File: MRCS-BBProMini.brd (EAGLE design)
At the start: 72.4 x 33.3 mm, 10 parts

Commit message: fixed silkscreen
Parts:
- BBLEO: value (none) -> Footprint
- C1: device SPCoast:e5-10.5 -> SPCoast:E5-10.5
- J1: value (none) -> 2.1mm
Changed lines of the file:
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@@
 <setting verticaltext="up"/>
 </settings>
-<grid distance="50" unitdist="mil" unit="mil" style="dots" multiple="2" display="yes" altdistance="25" altunitdist="mil" altunit="mil"/>
+<grid distance="50" unitdist="mil" unit="mm" style="dots" multiple="2" display="yes" altdistance="25" altunitdist="mil" altunit="mil"/>
 <layers>
 <layer number="1" name="Top" color="4" fill="1" visible="yes" active="yes"/>
@@
 <elements>
 <element name="OSHW1" library="SPCoast" package="OSHW-LOGO-M" value="DOC-OSHW-LOGO-M" x="34.29" y="11.43" smashed="yes"/>
-<element name="J1" library="SPCoast" package="DCJ0202" value="" x="8.89" y="9.525" smashed="yes" rot="R270"/>
+<element name="J1" library="SPCoast" package="DCJ0202" value="2.1mm" x="8.89" y="9.525" smashed="yes" rot="R270"/>
 <element name="LABEL1" library="SPCoast" package="PWR_LABEL" value="7-12vDC" x="20.32" y="6.985" smashed="yes" rot="R90">
 <attribute name="VALUE" x="15.494" y="3.937" size="1.27" layer="51"/>
@@
 <attribute name="VALUE" x="6.0325" y="29.21" size="1.27" layer="27" ratio="10"/>
 </element>
-<element name="C1" library="SPCoast" package="e5-10.5" value="150uF" x="15.875" y="18.415" smashed="yes" rot="R90">
+<element name="C1" library="SPCoast" package="E5-10.5" value="150uF" x="15.875" y="18.415" smashed="yes" rot="R90">
 <attribute name="NAME" x="14.17" y="16.845" size="1.27" layer="25" rot="R180"/>
 <attribute name="VALUE" x="19.05" y="19.05" size="1.27" layer="27" rot="R180"/>
 </element>
-<element name="BBLEO" library="SPCoast" package="ARDUINO-BBLEO" value="" x="0" y="0" smashed="yes"/>
+<element name="BBLEO" library="SPCoast" package="ARDUINO-BBLEO" value="Footprint" x="0" y="0" smashed="yes"/>
 <element name="ARDUINO1" library="SPCoast" package="ARDUINO_PRO_MINI_DAVEK" value="ARDUINO-PRO-MINIDAVESROBOT" x="39.37" y="26.67" smashed="yes" rot="R270"/>
 <element name="JP1" library="SPCoast" package="SJ_2S-NO" value="" x="60.96" y="4.445" smashed="yes" rot="R90">

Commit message: fixed silkscreen
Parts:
- JP1: value (none) -> OFF
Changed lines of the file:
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@@
 <setting verticaltext="up"/>
 </settings>
-<grid distance="50" unitdist="mil" unit="mm" style="dots" multiple="2" display="yes" altdistance="25" altunitdist="mil" altunit="mil"/>
+<grid distance="50" unitdist="mil" unit="mil" style="dots" multiple="2" display="yes" altdistance="25" altunitdist="mil" altunit="mil"/>
 <layers>
 <layer number="1" name="Top" color="4" fill="1" visible="yes" active="yes"/>
@@
 <element name="BBLEO" library="SPCoast" package="ARDUINO-BBLEO" value="Footprint" x="0" y="0" smashed="yes"/>
 <element name="ARDUINO1" library="SPCoast" package="ARDUINO_PRO_MINI_DAVEK" value="ARDUINO-PRO-MINIDAVESROBOT" x="39.37" y="26.67" smashed="yes" rot="R270"/>
-<element name="JP1" library="SPCoast" package="SJ_2S-NO" value="" x="60.96" y="4.445" smashed="yes" rot="R90">
+<element name="JP1" library="SPCoast" package="SJ_2S-NO" value="OFF" x="60.96" y="4.445" smashed="yes" rot="R90">
 <attribute name="NAME" x="59.69" y="3.537" size="0.4064" layer="25" rot="R90"/>
 <attribute name="VALUE" x="62.611" y="3.537" size="0.4064" layer="27" rot="R90"/>

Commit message: normalized values
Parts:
- ARDUINO1: value ARDUINO-PRO-MINIDAVESROBOT -> DAVEK
- OSHW1: value DOC-OSHW-LOGO-M -> OSHW

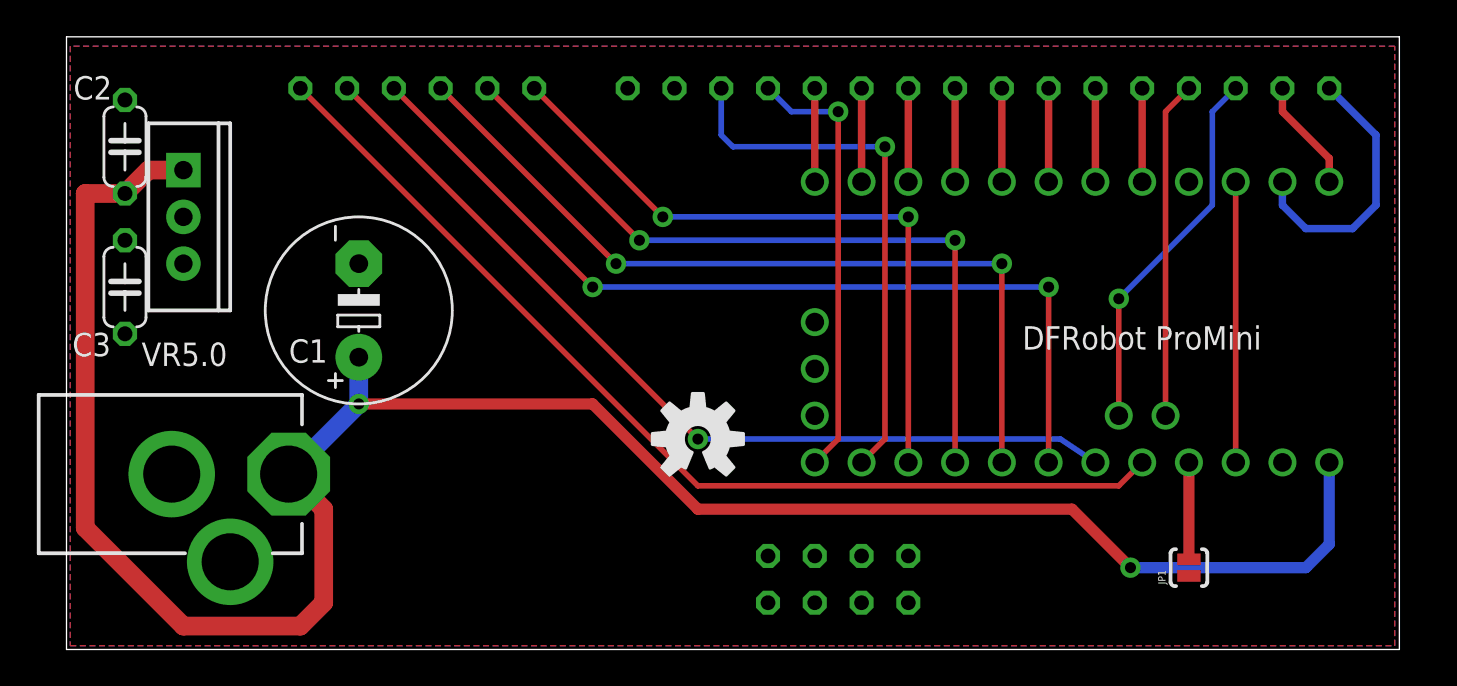
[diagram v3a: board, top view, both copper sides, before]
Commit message: Add 2k2 pullup to pin13
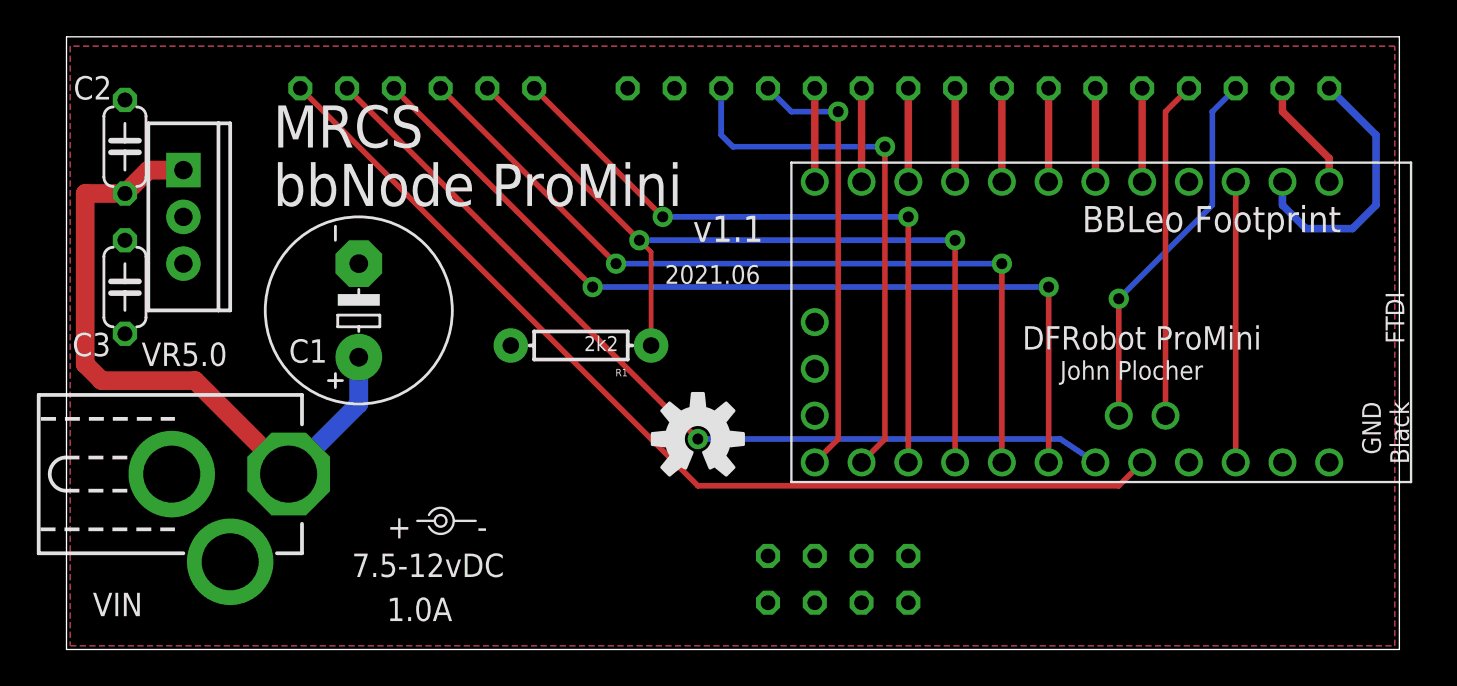
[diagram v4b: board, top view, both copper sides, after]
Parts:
- removed JP1: OFF, SPCoast:SJ_2S-NO
- added R1: 2k2, SPCoast:AXIAL-0.3-RES
- LABEL1: value 7-12vDC -> 7.5-12vDC
- VR5.0: device SPCoast:TO-220-RA-SINK -> SPCoast:TO-220-RA
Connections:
- removed net N$1: ARDUINO1.5V, JP1.2
- net +9V: no longer ARDUINO1.VIN
- net GPB3: now also R1.P$1
- net VCCIO: now also ARDUINO1.5V, R1.P$2; no longer JP1.1
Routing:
- net +9V: track 116.8 -> 36.6 mm, vias 2 -> 0
- net GPB3: track 40.9 -> 46.9 mm
- net N$1: track 5.27 -> 0.00 mm
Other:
- board text added: "2021.06"
- board text added: "v1.1"
- board text removed: "2019.08"
- board text removed: "v1.0"
